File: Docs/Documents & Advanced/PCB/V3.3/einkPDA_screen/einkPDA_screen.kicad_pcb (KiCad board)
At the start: 2 copper layers, 95 x 54 mm, 28 parts, among them J3 CapacitiveTouch, J4 Conn_01x12_Pin, Q1 Si1308EDL, U1 MPR121QR2

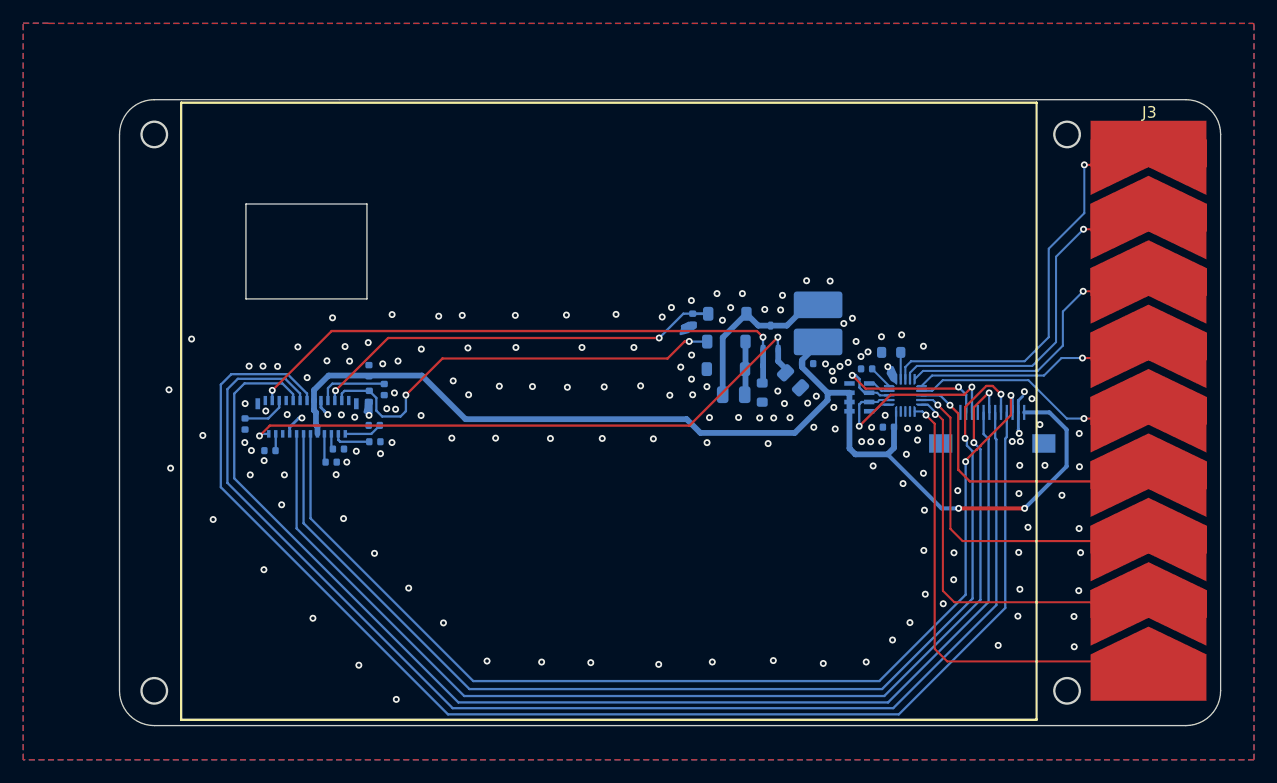
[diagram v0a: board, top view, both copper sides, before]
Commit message: Update Screen PCB Silkscreens
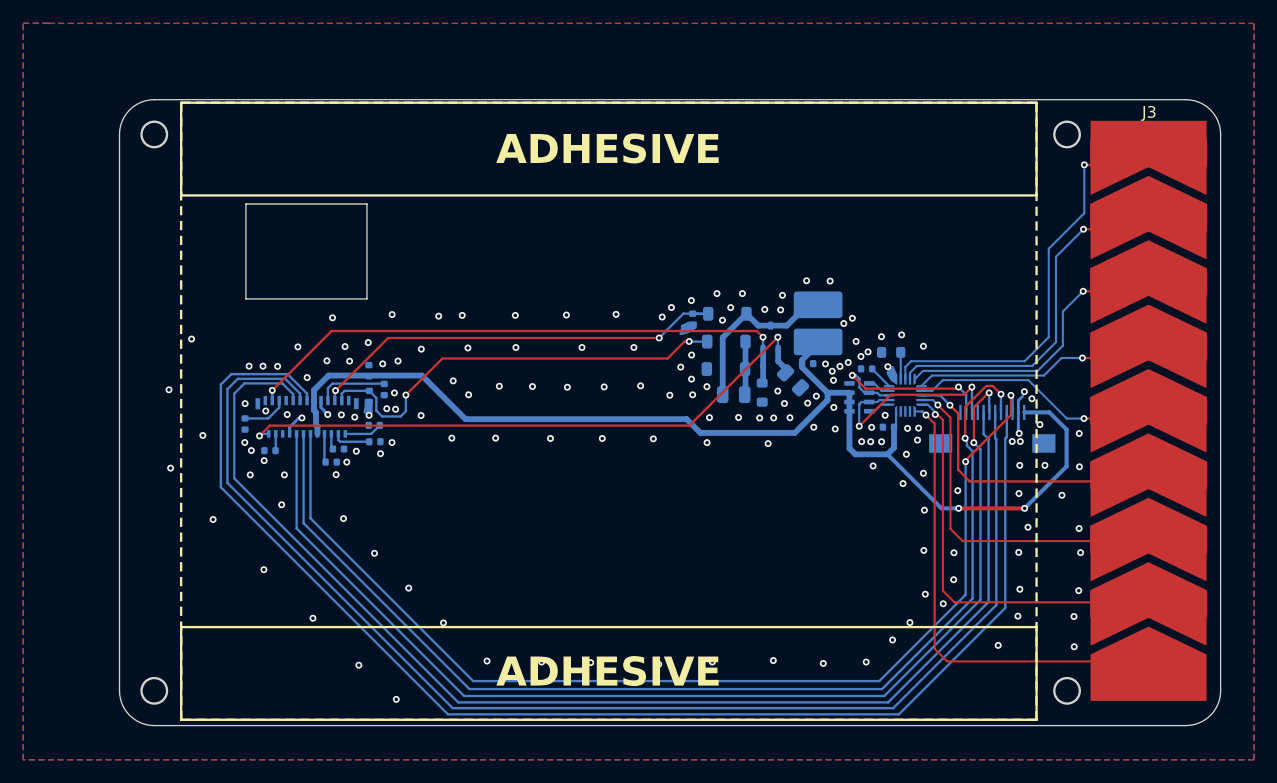
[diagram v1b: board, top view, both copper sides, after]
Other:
- board text added: "@Ashtf // V3.4"
- board text added: "ADHESIVE"
- board text added: "By Talisman Design"
- board text removed: "@Ashtf // V3.3"
